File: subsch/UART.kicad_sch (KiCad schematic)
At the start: 16 parts, among them Q2 Q_PNP_BCE, Q3 Q_PNP_BCE, Q4 Q_PNP_BCE, Q5 Q_PNP_BCE, U7 CH340E

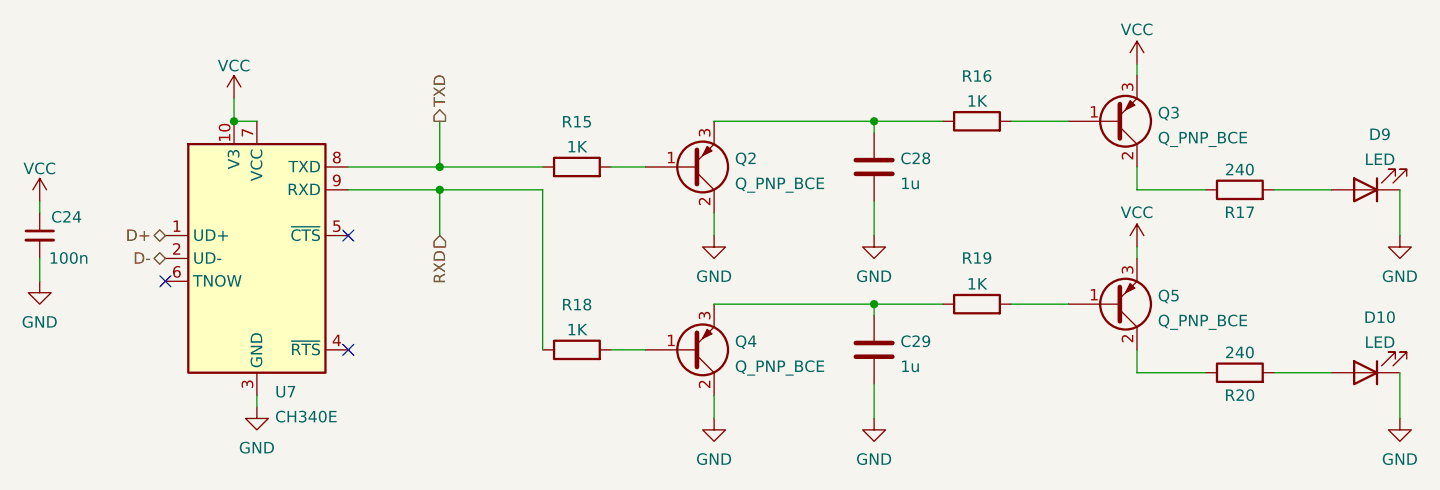
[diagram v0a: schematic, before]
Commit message: Change connectors back to GH1.25&Add ESD for UART and CAN
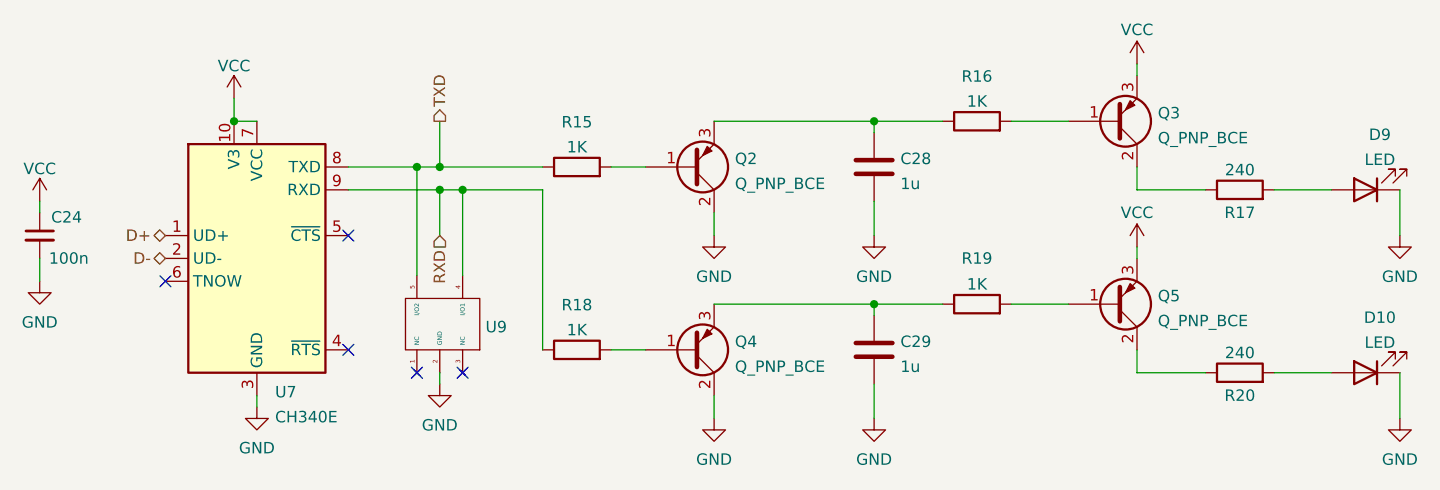
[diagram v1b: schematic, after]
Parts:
- added U9: ~, Package_TO_SOT_SMD:SOT-23-5, symbol Extra IC:ESDS314
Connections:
- net GND: now also U9.2 (GND)
- net RXD: now also U9.4 (I/O1)
- net TXD: now also U9.5 (I/O2)
- no-connect marks 3 -> 5
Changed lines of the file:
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@@
 (kicad_sch (version 20230121) (generator eeschema)
   (paper "A4")
+  (junction (at 158.75 77.47) (diameter 0) (color 0 0 0 0)
+  )
   (junction (at 138.43 72.39) (diameter 0) (color 0 0 0 0)
   )
@@
   (junction (at 209.55 92.71) (diameter 0) (color 0 0 0 0)
   )
+  (junction (at 163.83 80.01) (diameter 0) (color 0 0 0 0)
+  )
   (junction (at 161.29 77.47) (diameter 0) (color 0 0 0 0)
   )
+  (no_connect (at 163.83 100.33))
   (no_connect (at 151.13 85.09))
   (no_connect (at 151.13 97.79))
   (no_connect (at 130.81 90.17))
+  (no_connect (at 158.75 100.33))
   (wire (pts (xy 191.77 92.71) (xy 209.55 92.71))
     (stroke (width 0) (type default))
@@
     (stroke (width 0) (type default))
   )
+  (wire (pts (xy 158.75 77.47) (xy 161.29 77.47))
+    (stroke (width 0) (type default))
+  )
   (wire (pts (xy 191.77 72.39) (xy 209.55 72.39))
     (stroke (width 0) (type default))
@@
     (stroke (width 0) (type default))
   )
+  (wire (pts (xy 161.29 101.6) (xy 161.29 100.33))
+    (stroke (width 0) (type default))
+  )
+  (wire (pts (xy 163.83 80.01) (xy 163.83 89.535))
+    (stroke (width 0) (type default))
+  )
   (wire (pts (xy 254 100.33) (xy 260.35 100.33))
     (stroke (width 0) (type default))
@@
     (stroke (width 0) (type default))
   )
+  (wire (pts (xy 163.83 80.01) (xy 172.72 80.01))
+    (stroke (width 0) (type default))
+  )
   (wire (pts (xy 238.76 100.33) (xy 246.38 100.33))
     (stroke (width 0) (type default))
@@
     (stroke (width 0) (type default))
   )
-  (wire (pts (xy 151.13 77.47) (xy 161.29 77.47))
-    (stroke (width 0) (type default))
-  )
-  (wire (pts (xy 161.29 80.01) (xy 172.72 80.01))
+  (wire (pts (xy 151.13 77.47) (xy 158.75 77.47))
+    (stroke (width 0) (type default))
+  )
+  (wire (pts (xy 161.29 80.01) (xy 163.83 80.01))
+    (stroke (width 0) (type default))
+  )
+  (wire (pts (xy 158.75 77.47) (xy 158.75 89.535))
     (stroke (width 0) (type default))
   )
@@
         (path "/e63e39d7-6ac0-4ffd-8aa3-1841a4541b55/180acaec-474d-43bb-b90b-d192d08c2de1"
           (reference "R15") (unit 1)
+        )
+      )
+    )
+  )
+  (symbol (lib_id "Extra IC:ESDS314") (at 161.29 95.25 180) (unit 1)
+    (in_bom yes) (on_board yes) (dnp no) (fields_autoplaced)
+    (property "Reference" "U9" (at 166.37 95.2493 0)
+      (effects (font (size 1.27 1.27)) (justify right))
+    )
+    (property "Value" "~" (at 161.29 104.14 0)
+      (effects (font (size 1.27 1.27)))
+    )
+    (property "Footprint" "Package_TO_SOT_SMD:SOT-23-5" (at 161.29 104.14 0)
+      (effects (font (size 1.27 1.27)) hide)
+    )
+    (property "Datasheet" "" (at 161.29 104.14 0)
+      (effects (font (size 1.27 1.27)) hide)
+    )
+    (pin "1")
+    (pin "2")
+    (pin "3")
+    (pin "4")
+    (pin "5")
+    (instances
+      (project "USB2XXX"
+        (path "/e63e39d7-6ac0-4ffd-8aa3-1841a4541b55/180acaec-474d-43bb-b90b-d192d08c2de1"
+          (reference "U9") (unit 1)
         )
       )
@@
         )
       )
+    )
+  )
+  (symbol (lib_id "power:GND") (at 161.29 101.6 0) (unit 1)
+    (in_bom yes) (on_board yes) (dnp no) (fields_autoplaced)
+    (property "Reference" "#PWR084" (at 161.29 107.95 0)
+      (effects (font (size 1.27 1.27)) hide)
+    )
+    (property "Value" "GND" (at 161.29 106.1625 0)
+      (effects (font (size 1.27 1.27)))
+    )
+    (property "Footprint" "" (at 161.29 101.6 0)
+      (effects (font (size 1.27 1.27)) hide)
+    )
+    (property "Datasheet" "" (at 161.29 101.6 0)
+      (effects (font (size 1.27 1.27)) hide)
+    )
+    (pin "1")
+    (instances
+      (project "USB2XXX"
+        (path "/e63e39d7-6ac0-4ffd-8aa3-1841a4541b55/180acaec-474d-43bb-b90b-d192d08c2de1"
+          (reference "#PWR084") (unit 1)
+        )
+      )

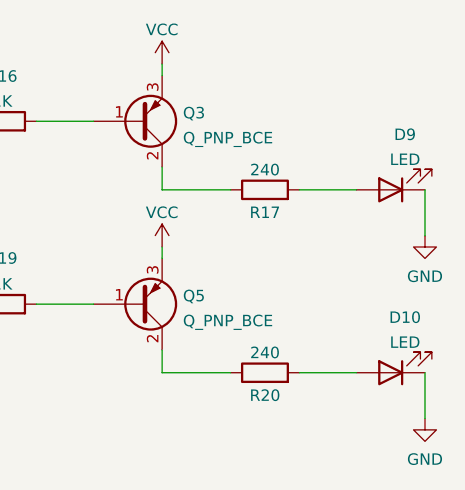
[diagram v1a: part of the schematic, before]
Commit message: Adaption for SMT
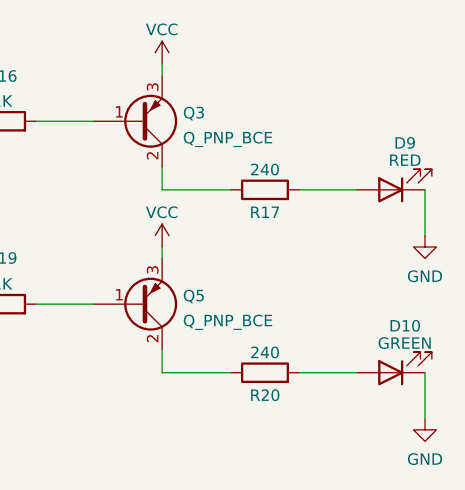
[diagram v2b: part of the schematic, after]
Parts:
- D10: value LED -> GREEN
- D9: value LED -> RED
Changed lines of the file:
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@@
   (symbol (lib_id "Device:LED") (at 264.16 100.33 180) (unit 1)
     (in_bom yes) (on_board yes) (dnp no) (fields_autoplaced)
-    (property "Reference" "D10" (at 265.7475 94.2045 0)
+    (property "Reference" "D10" (at 265.7475 95.1611 0)
       (effects (font (size 1.27 1.27)))
     )
-    (property "Value" "LED" (at 265.7475 96.9796 0)
+    (property "Value" "GREEN" (at 265.7475 97.0821 0)
       (effects (font (size 1.27 1.27)))
     )
@@
   (symbol (lib_id "Device:LED") (at 264.16 80.01 180) (unit 1)
     (in_bom yes) (on_board yes) (dnp no) (fields_autoplaced)
-    (property "Reference" "D9" (at 265.7475 73.8845 0)
+    (property "Reference" "D9" (at 265.7475 74.8411 0)
       (effects (font (size 1.27 1.27)))
     )
-    (property "Value" "LED" (at 265.7475 76.6596 0)
+    (property "Value" "RED" (at 265.7475 76.7621 0)
       (effects (font (size 1.27 1.27)))
     )

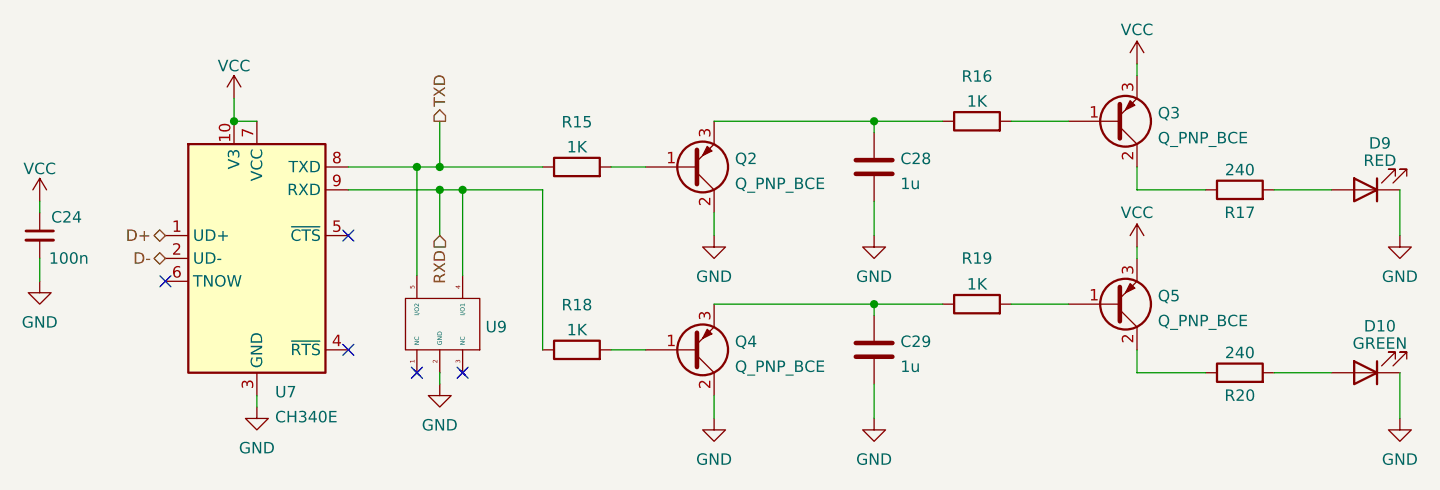
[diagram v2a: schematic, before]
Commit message: Adaption for SMT(hotfix)
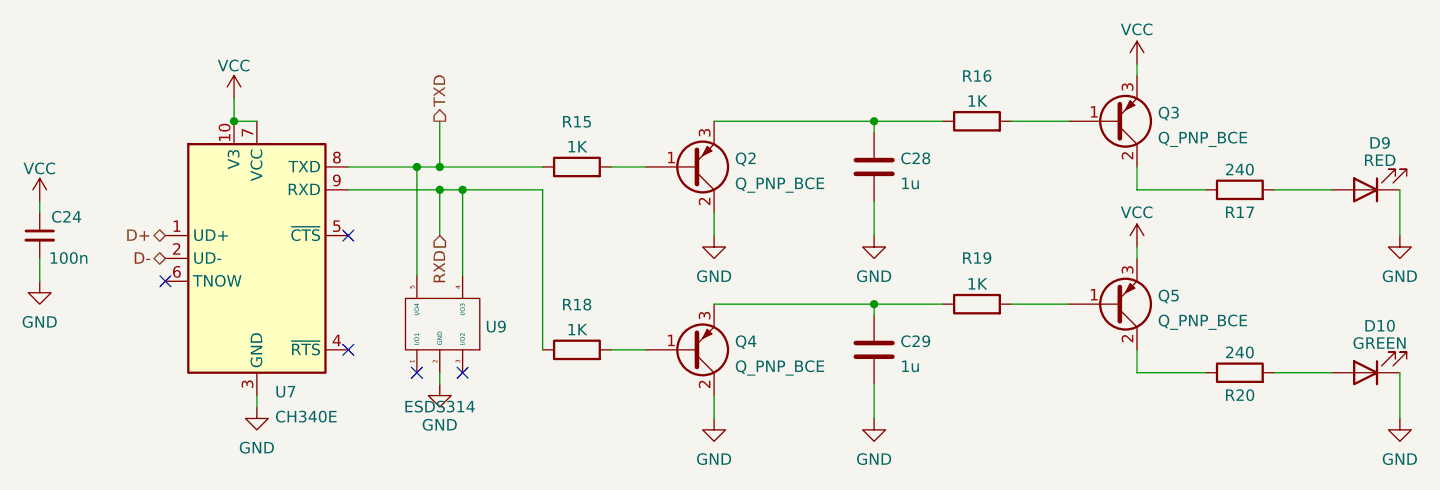
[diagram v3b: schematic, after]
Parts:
- U9: value ~ -> ESDS314
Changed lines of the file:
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@@
       (effects (font (size 1.27 1.27)) (justify right))
     )
-    (property "Value" "~" (at 161.29 104.14 0)
+    (property "Value" "ESDS314" (at 161.29 104.14 0)
       (effects (font (size 1.27 1.27)))
     )
-    (property "Footprint" "Package_TO_SOT_SMD:SOT-23-5" (at 161.29 104.14 0)
+    (property "Footprint" "Package_TO_SOT_SMD:SOT-23-5" (at 161.29 94.615 0)
       (effects (font (size 1.27 1.27)) hide)
     )
-    (property "Datasheet" "" (at 161.29 104.14 0)
+    (property "Datasheet" "" (at 161.29 94.615 0)
       (effects (font (size 1.27 1.27)) hide)
     )
